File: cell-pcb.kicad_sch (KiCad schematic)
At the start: 46 parts, among them J1 TC2030, J10 Conn_01x01, J11 Conn_01x01, J12 Conn_01x01, J13 Conn_01x01, J14 Conn_01x01, J2 Conn_01x01, J28 Conn_01x04, J3 Conn_01x01, J31 DA15_Receptacle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

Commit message: more layout and memes
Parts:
- C10, C12, C7, C8, C9: LibRef (none) -> CL10B104KB8NNNC; SKU (none) -> CL10B104KB8NNNC; Supplier (none) -> Digikey
- C11: LibRef (none) -> CL10A105KA8NNNC; SKU (none) -> CL10A105KA8NNNC; Supplier (none) -> Digikey
- C14, C15: LibRef (none) -> CML0603C0G300JT50V; SKU (none) -> CML0603C0G300JT50V; Supplier (none) -> Digikey
- C6: LibRef (none) -> CL10A475KP8NNNC; SKU (none) -> CL10A475KP8NNNC; Supplier (none) -> Digikey
- D19: value RED -> RED 0603; LibRef (none) -> B1911USD-20D000114U1930; SKU (none) -> B1911USD-20D000114U1930; Supplier (none) -> Digikey
- F1, F10, F11, F12, F13, F2, F3, F4, F5, F6, F7, F8, F9: value Fuse -> 2A 63VDC 1206; LibRef (none) -> 0685T2000-01; SKU (none) -> 0685T2000-01; Supplier (none) -> Digikey
- FB1: LibRef (none) -> 2508051017Y0; SKU (none) -> 2508051017Y0; Supplier (none) -> Digikey
- J10, J11, J12, J13, J14, J2, J3, J4, J5, J6, J7, J8, J9: value Conn_01x01 -> Mounting Hole M5; now left out of the parts list
- J28: value Conn_01x04 -> Pin Header 0.1" 01x04; now left out of the parts list
- J31: value DA15_Receptacle -> 172-015-243R021; SKU (none) -> 172-015-243R021; Supplier (none) -> Digikey
- U5: value STM32F103R8Tx -> STM32F103R8T6; LibRef (none) -> STM32F103R8T6TR; SKU (none) -> STM32F103R8T6TR; Supplier (none) -> Digikey
- Y1: value 8MHz -> 8MHz 20pF; LibRef (none) -> XR19M66080S420; SKU (none) -> XR19M66080S420; Supplier (none) -> Digikey

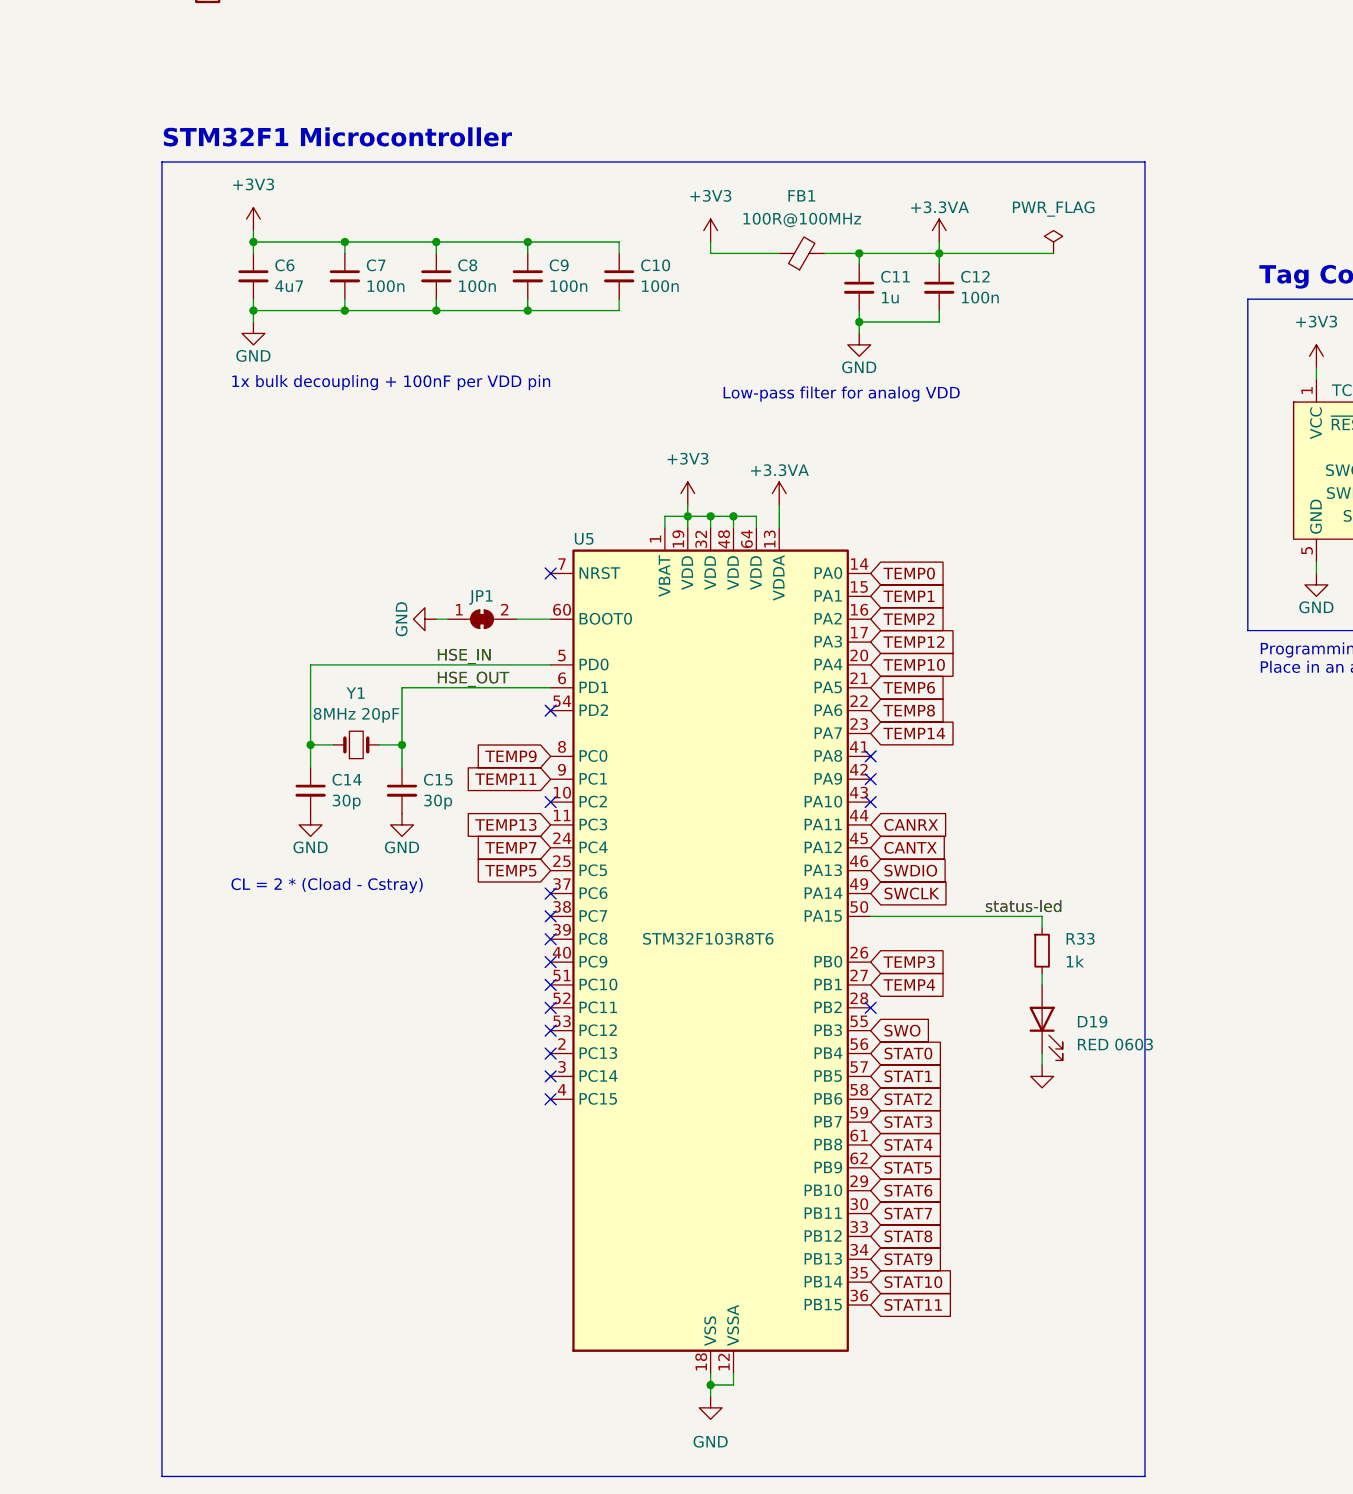
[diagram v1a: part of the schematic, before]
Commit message: removed slots
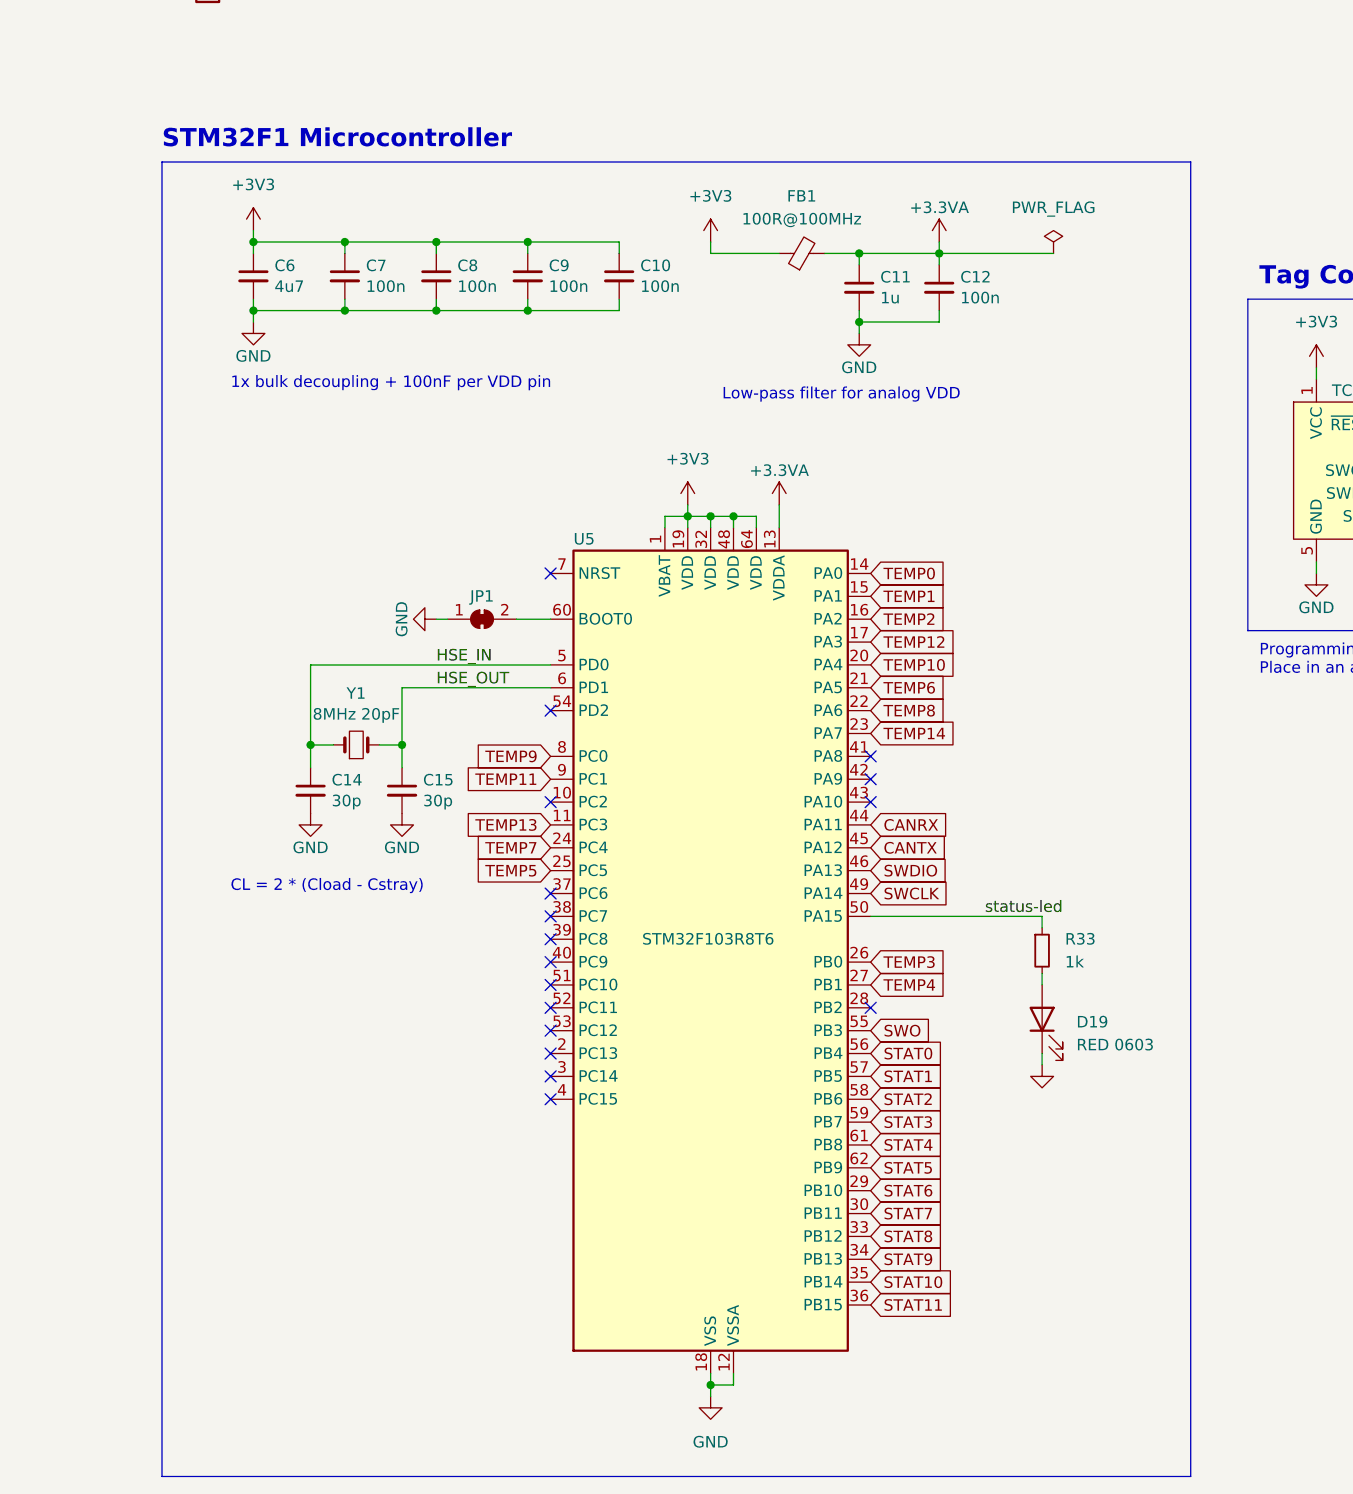
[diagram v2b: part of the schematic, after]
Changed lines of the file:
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@@
     (stroke (width 0) (type default))
   )
-  (polyline (pts (xy 196.85 270.51) (xy 196.85 124.46))
+  (polyline (pts (xy 201.93 270.51) (xy 201.93 124.46))
     (stroke (width 0) (type default))
   )
-  (polyline (pts (xy 196.85 124.46) (xy 87.63 124.46))
+  (polyline (pts (xy 201.93 124.46) (xy 87.63 124.46))
     (stroke (width 0) (type default))
   )
@@
     (stroke (width 0) (type default))
   )
-  (polyline (pts (xy 87.63 270.51) (xy 196.85 270.51))
+  (polyline (pts (xy 87.63 270.51) (xy 201.93 270.51))
     (stroke (width 0) (type default))
   )
